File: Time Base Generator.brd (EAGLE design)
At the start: 100 x 80 mm, 8 parts, among them IC1 4060N, IC2 4013N, X1_32768 CRYSTALS-NOGND-WATCH-3X8

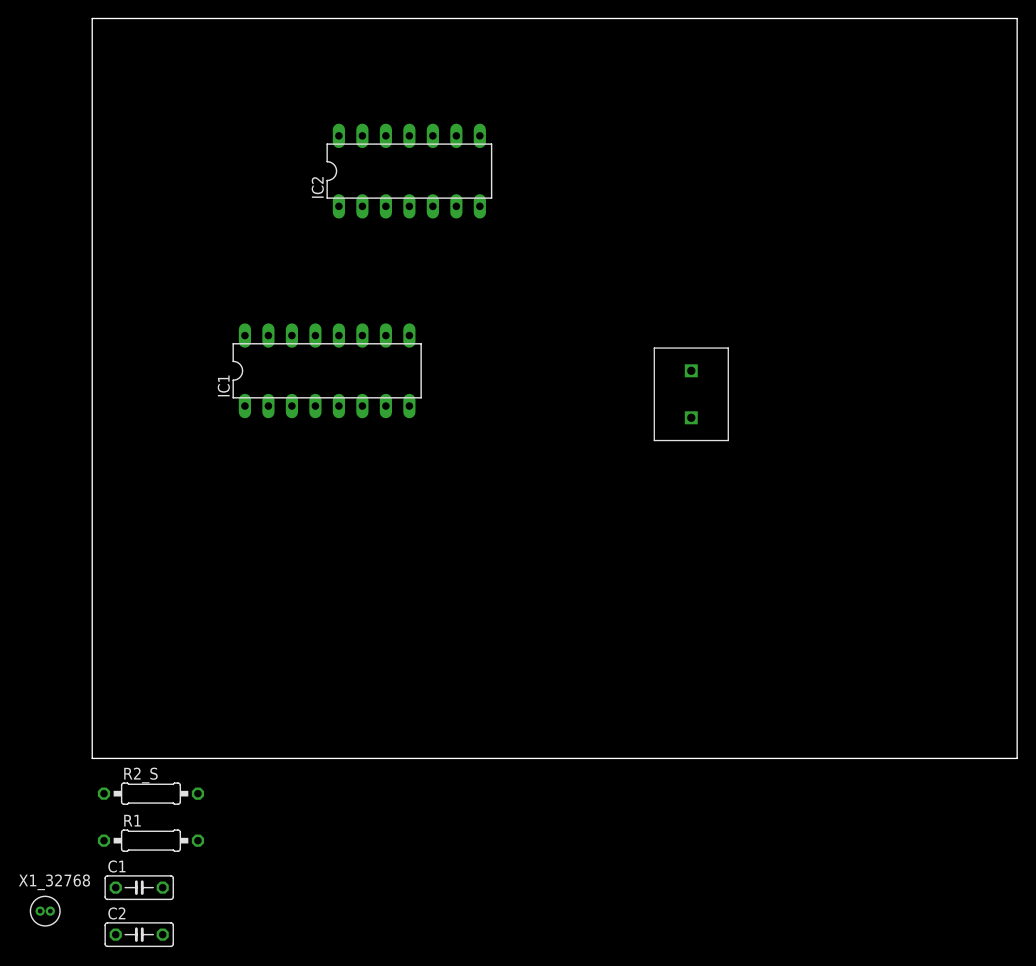
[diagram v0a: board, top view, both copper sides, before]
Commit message: Add TubeAlt, rename Control Logic, use jumper
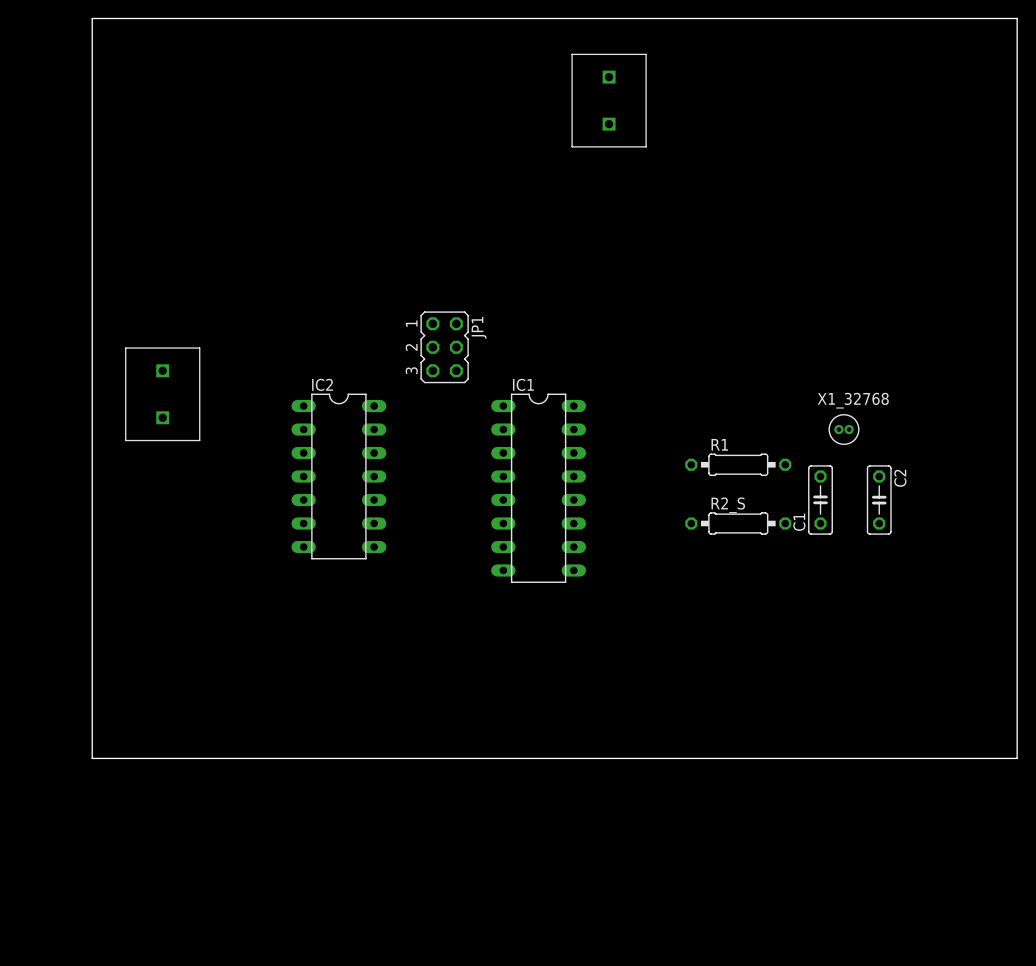
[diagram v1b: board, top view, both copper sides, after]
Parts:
- added JP1: (no value), jumper:JP3Q
- added OUTPUT: CON_2_SIL, PGT:SIL_2_0.2INCH
- moved X1_32768 100.8 mm to (81.3, 35.6)
- moved C2 92.8 mm to (85.1, 27.9), turned to 270 degrees
- moved C1 84.7 mm to (78.7, 27.9), turned to 90 degrees
- moved R1 75.4 mm to (69.8, 31.8)
- moved R2_S 69.9 mm to (69.8, 25.4)
- moved POWER_SUPPY 57.1 mm to (7.62, 39.4)
- moved IC2 33.9 mm to (26.7, 30.5), turned to 270 degrees
- moved IC1 26.2 mm to (48.3, 29.2), turned to 270 degrees
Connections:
- new net N$6: IC1.2, JP1.4
- net 2_HZ: now also JP1.6
- net 8_HZ: now also JP1.2
- net GND: now also OUTPUT.P$2
- net N$1: no longer IC1.11
- net TIME_REFERENCE: now also OUTPUT.P$1
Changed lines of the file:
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@@
 </autorouter>
 <elements>
-<element name="IC1" library="40xx" package="DIL16" value="4060N" x="25.4" y="41.91"/>
-<element name="R2_S" library="resistor" package="0207/10" value="220k" x="6.35" y="-3.81"/>
-<element name="R1" library="resistor" package="0207/10" value="10M" x="6.35" y="-8.89"/>
-<element name="C1" library="resistor" package="C050-025X075" value="25p" x="5.08" y="-13.97"/>
-<element name="C2" library="resistor" package="C050-025X075" value="25p" x="5.08" y="-19.05"/>
-<element name="X1_32768" library="IQD-Frequency-Products" package="WATCH-3X8" value="CRYSTALS-NOGND-WATCH-3X8" x="-5.08" y="-16.51"/>
-<element name="IC2" library="40xx" package="DIL14" value="4013N" x="34.29" y="63.5"/>
-<element name="POWER_SUPPY" library="PGT" package="SIL_2_0.2INCH" value="CON_2_SIL" x="64.77" y="39.37"/>
+<element name="IC1" library="40xx" package="DIL16" value="4060N" x="48.26" y="29.21" rot="R270"/>
+<element name="R2_S" library="resistor" package="0207/10" value="220k" x="69.85" y="25.4"/>
+<element name="R1" library="resistor" package="0207/10" value="10M" x="69.85" y="31.75"/>
+<element name="C1" library="resistor" package="C050-025X075" value="25p" x="78.74" y="27.94" rot="R90"/>
+<element name="C2" library="resistor" package="C050-025X075" value="25p" x="85.09" y="27.94" rot="R270"/>
+<element name="X1_32768" library="IQD-Frequency-Products" package="WATCH-3X8" value="CRYSTALS-NOGND-WATCH-3X8" x="81.28" y="35.56"/>
+<element name="IC2" library="40xx" package="DIL14" value="4013N" x="26.67" y="30.48" rot="R270"/>
+<element name="POWER_SUPPY" library="PGT" package="SIL_2_0.2INCH" value="CON_2_SIL" x="7.62" y="39.37"/>
+<element name="OUTPUT" library="PGT" package="SIL_2_0.2INCH" value="CON_2_SIL" x="55.88" y="71.12"/>
+<element name="JP1" library="jumper" package="JP3Q" value="" x="38.1" y="44.45" rot="R270"/>
 </elements>
 <signals>
@@
 <contactref element="IC1" pad="8"/>
 <contactref element="IC2" pad="7"/>
-<wire x1="34.29" y1="38.1" x2="41.91" y2="59.69" width="0" layer="19" extent="1-1"/>
+<wire x1="22.86" y1="22.86" x2="44.45" y2="20.32" width="0" layer="19" extent="1-1"/>
 </signal>
 <signal name="VDD">
@@
 <contactref element="IC2" pad="14"/>
 <contactref element="POWER_SUPPY" pad="P$1"/>
-<wire x1="26.67" y1="67.31" x2="64.77" y2="41.91" width="0" layer="19" extent="1-1"/>
-<wire x1="16.51" y1="45.72" x2="26.67" y2="67.31" width="0" layer="19" extent="1-1"/>
+<wire x1="30.48" y1="38.1" x2="52.07" y2="38.1" width="0" layer="19" extent="1-1"/>
+<wire x1="7.62" y1="41.91" x2="30.48" y2="38.1" width="0" layer="19" extent="1-1"/>
+</signal>
+<signal name="GND">
+<contactref element="POWER_SUPPY" pad="P$2"/>
+<contactref element="IC2" pad="6"/>
+<contactref element="IC2" pad="4"/>
+<contactref element="OUTPUT" pad="P$2"/>
+<contactref element="C2" pad="2"/>
+<contactref element="C1" pad="1"/>
+<contactref element="IC1" pad="12"/>
+<wire x1="52.07" y1="27.94" x2="55.88" y2="68.58" width="0" layer="19" extent="1-1"/>
+<wire x1="78.74" y1="25.4" x2="52.07" y2="27.94" width="0" layer="19" extent="1-1"/>
+<wire x1="85.09" y1="25.4" x2="78.74" y2="25.4" width="0" layer="19" extent="1-1"/>
+<wire x1="22.86" y1="30.48" x2="52.07" y2="27.94" width="0" layer="19" extent="1-1"/>
+<wire x1="22.86" y1="25.4" x2="22.86" y2="30.48" width="0" layer="19" extent="1-1"/>
+<wire x1="7.62" y1="36.83" x2="22.86" y2="30.48" width="0" layer="19" extent="1-1"/>
+</signal>
+<signal name="8_HZ">
+<contactref element="IC1" pad="1"/>
+<contactref element="JP1" pad="2"/>
+<wire x1="39.37" y1="46.99" x2="44.45" y2="38.1" width="0" layer="19" extent="1-1"/>
+</signal>
+<signal name="TIME_REFERENCE">
+<contactref element="IC2" pad="1"/>
+<contactref element="OUTPUT" pad="P$1"/>
+<wire x1="22.86" y1="38.1" x2="55.88" y2="73.66" width="0" layer="19" extent="1-1"/>
+</signal>
+<signal name="N$5">
+<contactref element="IC2" pad="2"/>
+<contactref element="IC2" pad="5"/>
+<wire x1="22.86" y1="27.94" x2="22.86" y2="35.56" width="0" layer="19" extent="1-1"/>
+</signal>
+<signal name="N$2">
+<contactref element="C1" pad="2"/>
+<contactref element="X1_32768" pad="1"/>
+<contactref element="R2_S" pad="2"/>
+<contactref element="R1" pad="2"/>
+<wire x1="78.74" y1="30.48" x2="80.73" y2="35.56" width="0" layer="19" extent="1-1"/>
+<wire x1="74.93" y1="31.75" x2="78.74" y2="30.48" width="0" layer="19" extent="1-1"/>
+<wire x1="74.93" y1="25.4" x2="78.74" y2="30.48" width="0" layer="19" extent="1-1"/>
 </signal>
 <signal name="N$1">
 <contactref element="C2" pad="1"/>
-<contactref element="IC1" pad="11"/>
 <contactref element="X1_32768" pad="2"/>
 <contactref element="R1" pad="1"/>
-<wire x1="1.27" y1="-8.89" x2="29.21" y2="45.72" width="0" layer="19" extent="1-1"/>
-<wire x1="-4.53" y1="-16.51" x2="1.27" y2="-8.89" width="0" layer="19" extent="1-1"/>
-<wire x1="2.54" y1="-19.05" x2="-4.53" y2="-16.51" width="0" layer="19" extent="1-1"/>
-</signal>
-<signal name="N$2">
-<contactref element="R1" pad="2"/>
-<contactref element="R2_S" pad="2"/>
-<contactref element="C1" pad="2"/>
-<contactref element="X1_32768" pad="1"/>
-<wire x1="7.62" y1="-13.97" x2="-5.63" y2="-16.51" width="0" layer="19" extent="1-1"/>
-<wire x1="11.43" y1="-8.89" x2="7.62" y2="-13.97" width="0" layer="19" extent="1-1"/>
-<wire x1="11.43" y1="-3.81" x2="11.43" y2="-8.89" width="0" layer="19" extent="1-1"/>
-</signal>
-<signal name="GND">
-<contactref element="C2" pad="2"/>
-<contactref element="C1" pad="1"/>
-<contactref element="IC1" pad="12"/>
-<contactref element="POWER_SUPPY" pad="P$2"/>
-<contactref element="IC2" pad="6"/>
-<contactref element="IC2" pad="4"/>
-<wire x1="39.37" y1="59.69" x2="64.77" y2="36.83" width="0" layer="19" extent="1-1"/>
-<wire x1="34.29" y1="59.69" x2="39.37" y2="59.69" width="0" layer="19" extent="1-1"/>
-<wire x1="26.67" y1="45.72" x2="34.29" y2="59.69" width="0" layer="19" extent="1-1"/>
-<wire x1="2.54" y1="-13.97" x2="26.67" y2="45.72" width="0" layer="19" extent="1-1"/>
-<wire x1="7.62" y1="-19.05" x2="2.54" y2="-13.97" width="0" layer="19" extent="1-1"/>
+<wire x1="85.09" y1="30.48" x2="81.83" y2="35.56" width="0" layer="19" extent="1-1"/>
+<wire x1="64.77" y1="31.75" x2="81.83" y2="35.56" width="0" layer="19" extent="1-1"/>
 </signal>
 <signal name="N$3">
 <contactref element="R2_S" pad="1"/>
 <contactref element="IC1" pad="10"/>
-<wire x1="1.27" y1="-3.81" x2="31.75" y2="45.72" width="0" layer="19" extent="1-1"/>
+<wire x1="52.07" y1="22.86" x2="64.77" y2="25.4" width="0" layer="19" extent="1-1"/>
+</signal>
+<signal name="N$6">
+<contactref element="IC1" pad="2"/>
+<contactref element="JP1" pad="4"/>
+<wire x1="39.37" y1="44.45" x2="44.45" y2="35.56" width="0" layer="19" extent="1-1"/>
 </signal>
 <signal name="2_HZ">
 <contactref element="IC1" pad="3"/>
-</signal>
-<signal name="8_HZ">
-<contactref element="IC1" pad="1"/>
+<contactref element="JP1" pad="6"/>
+<wire x1="39.37" y1="41.91" x2="44.45" y2="33.02" width="0" layer="19" extent="1-1"/>
 </signal>
 <signal name="N$4">
 <contactref element="IC2" pad="3"/>
 </signal>
-<signal name="TIME_REFERENCE">
-<contactref element="IC2" pad="1"/>
-</signal>
-<signal name="N$5">
-<contactref element="IC2" pad="2"/>
-<contactref element="IC2" pad="5"/>
-<wire x1="29.21" y1="59.69" x2="36.83" y2="59.69" width="0" layer="19" extent="1-1"/>
-</signal>
 </signals>

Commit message: Separate board for time reference generator
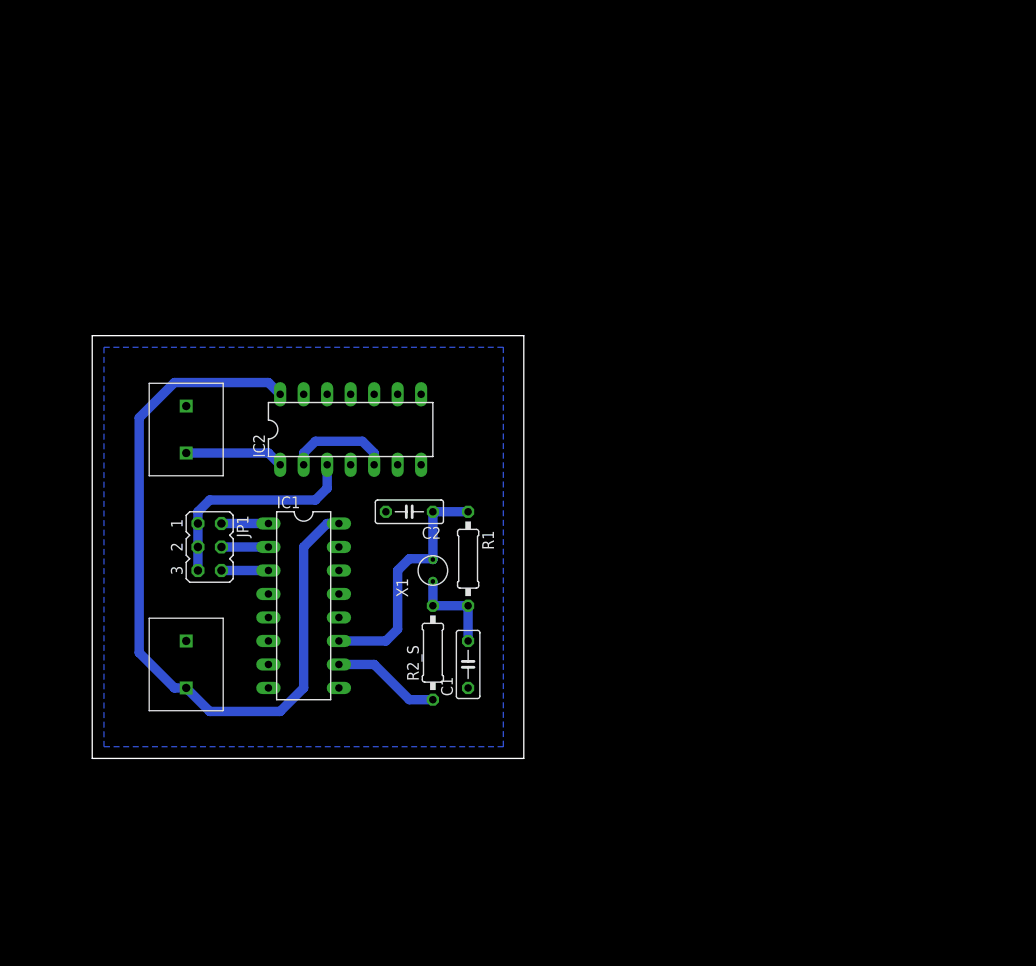
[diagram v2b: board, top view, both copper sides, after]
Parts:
- removed X1_32768: CRYSTALS-NOGND-WATCH-3X8, IQD-Frequency-Products:WATCH-3X8
- added X1: CRYSTAL_TINY, PGT:WATCH-3X8-SPACED
- JP1: value (none) -> FREQ_SELECT
- moved OUTPUT 57.9 mm to (10.2, 35.6), turned to 180 degrees
- moved C2 50.8 mm to (34.3, 26.7), turned to 180 degrees
- moved C1 42.0 mm to (40.6, 10.2)
- moved R2_S 35.9 mm to (36.8, 11.4), turned to 90 degrees
- moved JP1 33.3 mm to (12.7, 22.9)
- moved R1 30.9 mm to (40.6, 21.6), turned to 270 degrees
- moved POWER_SUPPY 29.3 mm to (10.2, 10.2), turned to 180 degrees
- moved IC1 28.4 mm to (22.9, 16.5)
- moved IC2 5.24 mm to (27.9, 35.6), turned to 0 degrees
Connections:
- net N$6 renamed 4_HZ
- removed net N$4: IC2.3
- removed net VSS: IC1.8, IC2.7
- new net N$8: IC2.3, JP1.1, JP1.3, JP1.5
- net GND: now also IC1.8, IC2.7
- net N$1: now also IC1.11, X1.2; no longer X1_32768.2
- net N$2: now also X1.1; no longer X1_32768.1
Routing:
- net VDD: track 0.00 -> 84.3 mm
- net N$1: track 0.00 -> 26.6 mm
- net N$8: track 0.00 -> 23.9 mm
- net N$3: track 0.00 -> 11.7 mm
- net N$5: track 0.00 -> 11.2 mm
- net TIME_REFERENCE: track 0.00 -> 10.7 mm
- net N$2: track 0.00 -> 10.2 mm
- net 8_HZ: track 0.00 -> 5.08 mm
- net 4_HZ: track 0.00 -> 5.08 mm
- net 2_HZ: track 0.00 -> 5.08 mm
- added copper zone on layer 16, net GND
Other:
- board size 100 x 80 mm -> 46.7 x 45.7 mm
